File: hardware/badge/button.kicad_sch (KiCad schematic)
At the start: 12 parts, among them SW601 TS-1187A-C-C-B, SW602 TS-1187A-C-C-B, SW603 TS-1187A-C-C-B, SW604 TS-1187A-C-C-B, SW605 TS-1187A-C-C-B, SW606 TS-1187A-C-C-B

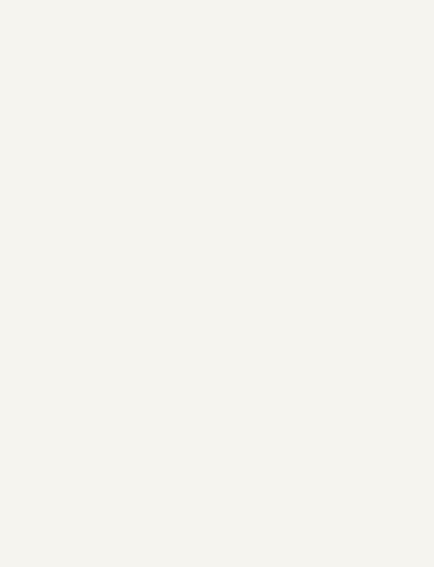
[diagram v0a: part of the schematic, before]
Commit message: feat: badge v2 PCB design with panelization support
Updated schematic and PCB layout for badge v2 revision. Added
panelization project with JLCPCB production files, panelize script,
and board SVG artwork.
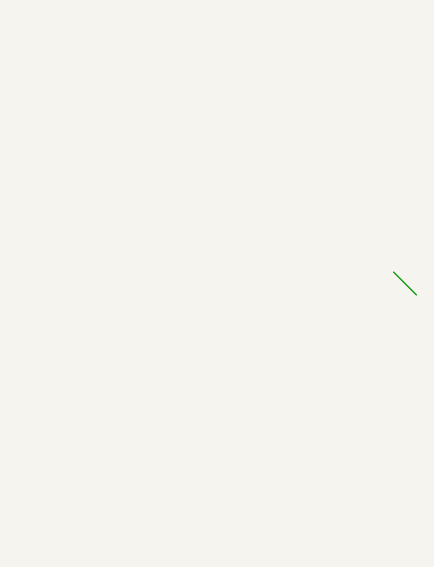
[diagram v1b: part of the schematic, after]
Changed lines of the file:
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@@
 		(color 0 0 0 0)
+	)
+	(bus_entry
+		(at 332.74 88.9)
+		(size 2.54 2.54)
+		(stroke
+			(width 0)
+			(type default)
+		)
 	)
 	(wire
@@
 			)
 		)
-		(property "Description" ""
+		(property "Description" "RIGHT"
 			(at 90.805 92.075 0)
 			(effects
@@
 			)
 		)
-		(property "Description" ""
+		(property "Description" "DOWN"
 			(at 90.805 57.785 0)
 			(effects
@@
 			)
 		)
-		(property "Description" ""
+		(property "Description" "LEFT"
 			(at 90.805 74.93 0)
 			(effects
@@
 			)
 		)
-		(property "Description" ""
+		(property "Description" "UP"
 			(at 90.805 41.275 0)
 			(effects
@@
 			)
 		)
-		(property "Description" ""
+		(property "Description" "A"
 			(at 90.805 109.22 0)
 			(effects
@@
 			)
 		)
-		(property "Description" ""
+		(property "Description" "B"
 			(at 90.805 127 0)
 			(effects
